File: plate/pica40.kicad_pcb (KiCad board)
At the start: 2 copper layers, 134 x 93.7 mm, 25 parts, among them SW1 SW_PUSH, SW10 SW_PUSH, SW11 SW_PUSH, SW12 SW_PUSH, SW13 SW_PUSH, SW14 SW_PUSH, SW15 SW_PUSH, SW16 SW_PUSH, SW17 SW_PUSH, SW18 SW_PUSH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

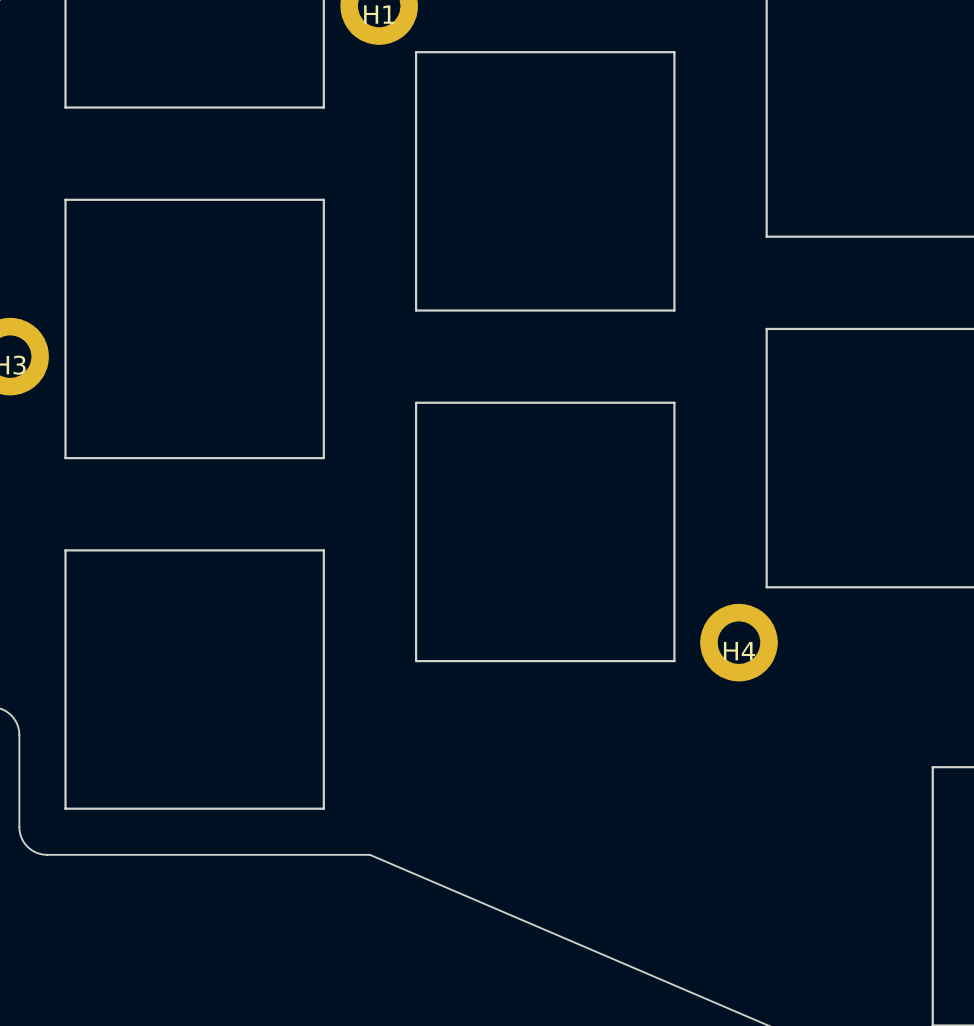
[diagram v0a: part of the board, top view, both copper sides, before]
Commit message: logos and jlcpcb texts
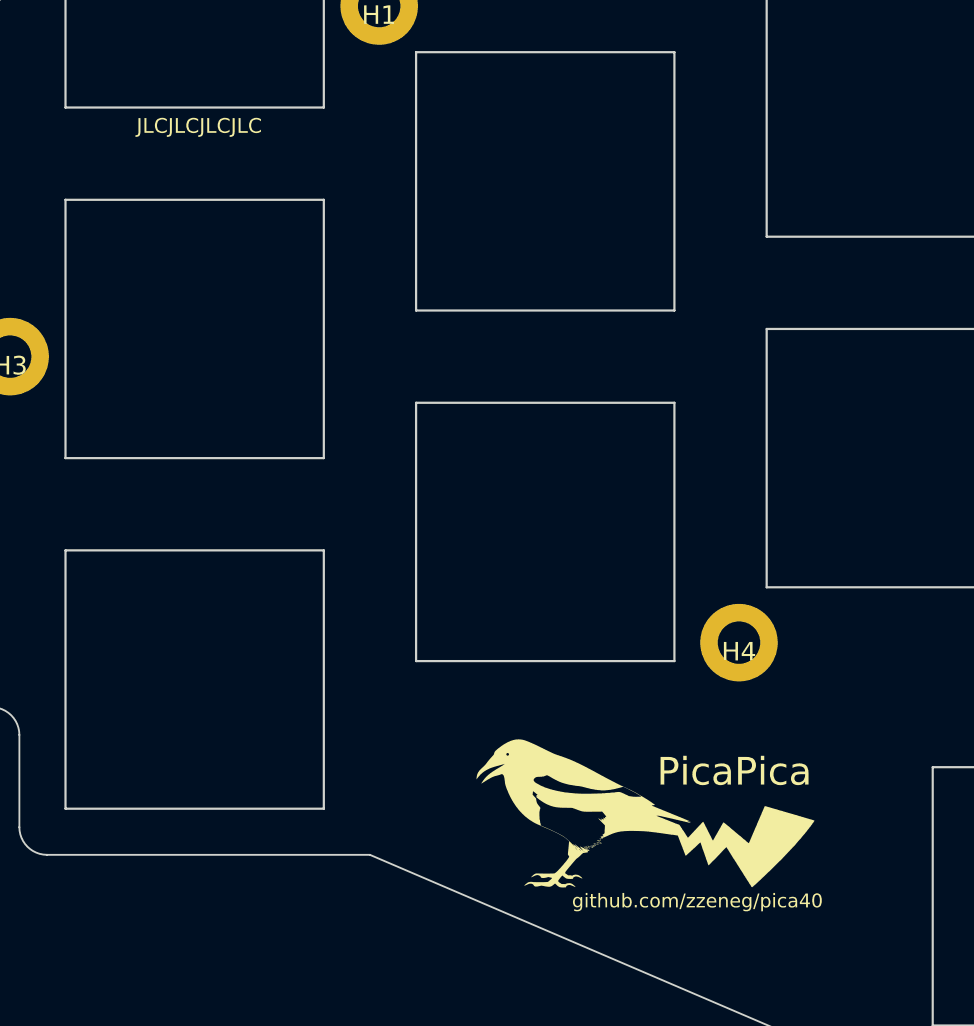
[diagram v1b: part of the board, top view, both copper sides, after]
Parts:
- added G***: LOGO, pica:logo, F.Cu at (120.8, 118.2)
- added G***: LOGO, pica:logo_mirror, B.Cu at (120.8, 118.2)
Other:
- board text added: "JLCJLCJLCJLC"
- board text added: "PicaPica"
- board text added: "github.com/zzeneg/pica40"
